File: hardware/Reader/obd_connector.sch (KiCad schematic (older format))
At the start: 2 parts

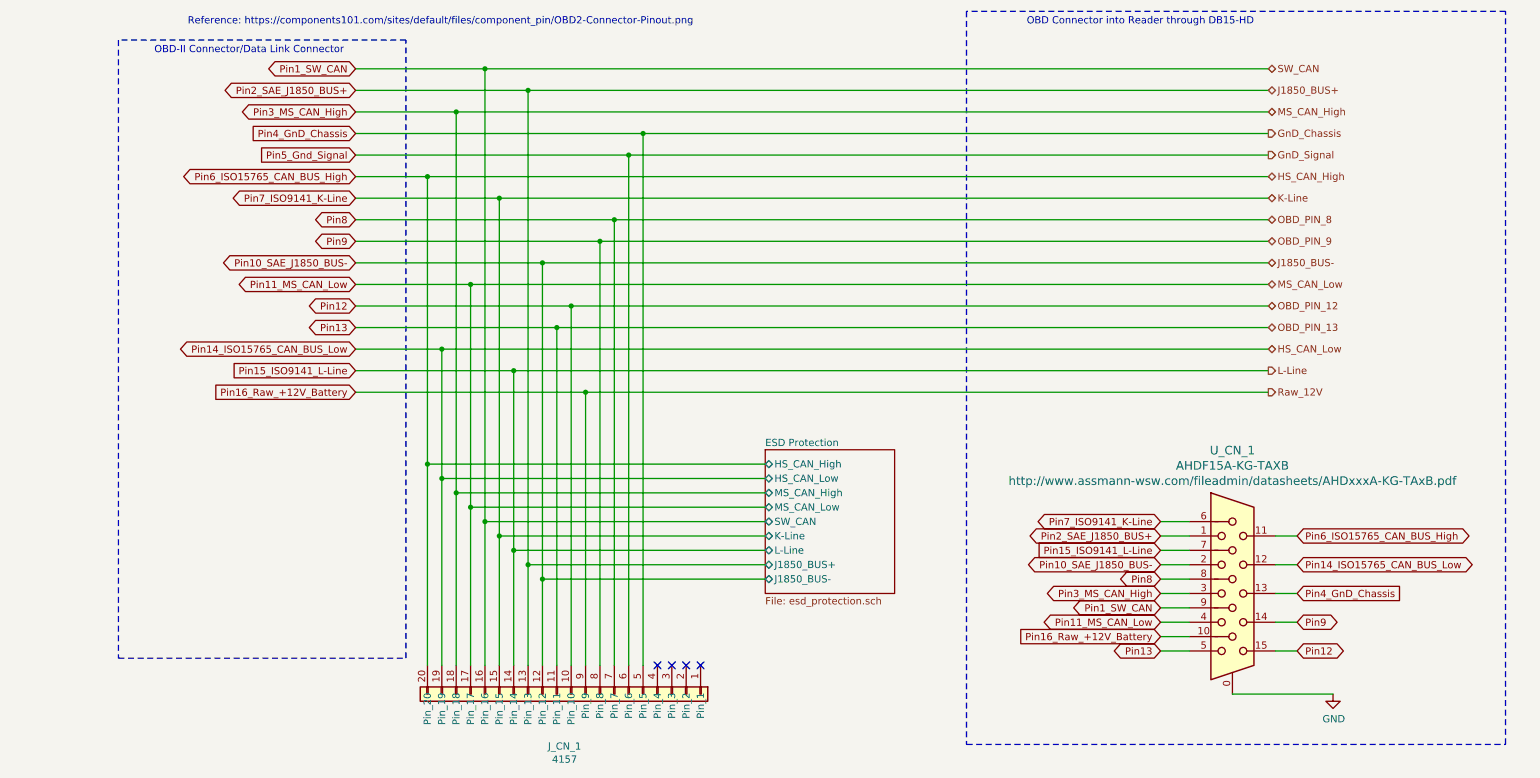
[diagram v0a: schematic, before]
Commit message: Updated reader schematic to v0.0.5 by adding ESP32, removing unused transceivers, fixed design flaws, increased header pins and fixed footprints. Working on reader PCB design
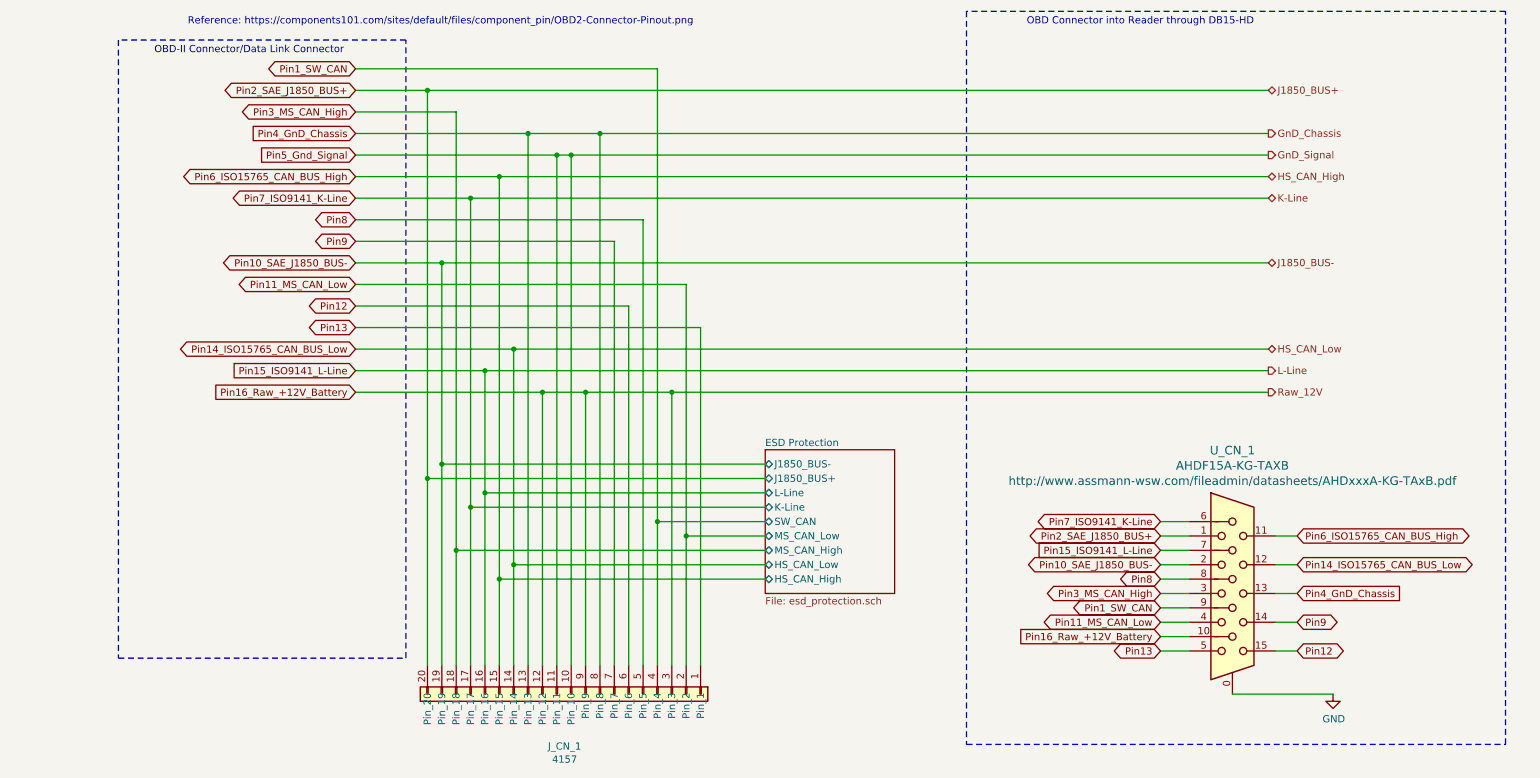
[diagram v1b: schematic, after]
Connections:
- net Pin10_SAE_J1850_BUS-: now also J_CN_1.19 (Pin_19); no longer J_CN_1.12 (Pin_12)
- net Pin11_MS_CAN_Low: now also J_CN_1.2 (Pin_2); no longer J_CN_1.17 (Pin_17)
- net Pin12: now also J_CN_1.6 (Pin_6); no longer J_CN_1.10 (Pin_10)
- net Pin13: now also J_CN_1.1 (Pin_1); no longer J_CN_1.11 (Pin_11)
- net Pin14_ISO15765_CAN_BUS_Low: now also J_CN_1.14 (Pin_14); no longer J_CN_1.19 (Pin_19)
- net Pin15_ISO9141_L-Line: now also J_CN_1.16 (Pin_16); no longer J_CN_1.14 (Pin_14)
- net Pin16_Raw_+12V_Battery: now also J_CN_1.12 (Pin_12), J_CN_1.3 (Pin_3)
- net Pin1_SW_CAN: now also J_CN_1.4 (Pin_4); no longer J_CN_1.16 (Pin_16)
- net Pin2_SAE_J1850_BUS+: now also J_CN_1.20 (Pin_20); no longer J_CN_1.13 (Pin_13)
- net Pin4_GnD_Chassis: now also J_CN_1.13 (Pin_13), J_CN_1.8 (Pin_8); no longer J_CN_1.5 (Pin_5)
- net Pin5_Gnd_Signal: now also J_CN_1.10 (Pin_10), J_CN_1.11 (Pin_11); no longer J_CN_1.6 (Pin_6)
- net Pin6_ISO15765_CAN_BUS_High: now also J_CN_1.15 (Pin_15); no longer J_CN_1.20 (Pin_20)
- net Pin7_ISO9141_K-Line: now also J_CN_1.17 (Pin_17); no longer J_CN_1.15 (Pin_15)
- net Pin8: now also J_CN_1.5 (Pin_5); no longer J_CN_1.7 (Pin_7)
- net Pin9: now also J_CN_1.7 (Pin_7); no longer J_CN_1.8 (Pin_8)
- no-connect marks 4 -> 0
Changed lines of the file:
@@
 $Descr USLetter 11000 8500
 encoding utf-8
-Sheet 11 19
+Sheet 10 17
 Title "CANnect Reader | OBD Connector"
-Date "2020-11-19"
+Date "2020-11-27"
 Rev "0.0.05"
 Comp "CANtech"
@@
 Comment4 "Component Identifier: CN"
 $EndDescr
-Text HLabel 8600 1550 2    50   BiDi ~ 0
-SW_CAN
 Text HLabel 8600 3800 2    50   Output ~ 0
 Raw_12V
 Text HLabel 8600 1700 2    50   BiDi ~ 0
 J1850_BUS+
-Text HLabel 8600 1850 2    50   BiDi ~ 0
-MS_CAN_High
 Text HLabel 8600 2000 2    50   Output ~ 0
 GnD_Chassis
@@
 Text HLabel 8600 2450 2    50   BiDi ~ 0
 K-Line
-Text HLabel 8600 2600 2    50   BiDi ~ 0
-OBD_PIN_8
-Text HLabel 8600 2750 2    50   BiDi ~ 0
-OBD_PIN_9
 Text HLabel 8600 2900 2    50   BiDi ~ 0
 J1850_BUS-
-Text HLabel 8600 3050 2    50   BiDi ~ 0
-MS_CAN_Low
-Text HLabel 8600 3200 2    50   BiDi ~ 0
-OBD_PIN_12
-Text HLabel 8600 3350 2    50   BiDi ~ 0
-OBD_PIN_13
 Text HLabel 8600 3500 2    50   BiDi ~ 0
 HS_CAN_Low
@@
 Wire Notes Line
 	10250 1150 6500 1150
-Wire Wire Line
-	2750 2300 2750 4300
-Wire Wire Line
-	2850 3500 2850 4400
-Wire Wire Line
-	2950 1850 2950 4500
-Wire Wire Line
-	2950 1850 8600 1850
-Wire Wire Line
-	3250 4800 3250 2450
 Wire Notes Line
 	10250 6250 10250 1150
-Connection ~ 2850 3500
-Connection ~ 2750 2300
-Connection ~ 2950 1850
-Wire Wire Line
-	2250 2900 3550 2900
-Wire Wire Line
-	2250 2000 4250 2000
-Wire Wire Line
-	2250 1850 2950 1850
 Text GLabel 2250 2600 0    50   BiDi ~ 0
 Pin8
@@
 Text GLabel 8800 5400 2    50   BiDi ~ 0
 Pin9
-Wire Wire Line
-	2250 2150 4150 2150
-Wire Wire Line
-	2250 2300 2750 2300
-Wire Wire Line
-	2250 2600 4050 2600
-Wire Wire Line
-	2250 2450 3250 2450
-Wire Wire Line
-	2250 3350 3650 3350
-Wire Wire Line
-	2250 3500 2850 3500
 Text GLabel 2250 3650 0    50   Input ~ 0
 Pin15_ISO9141_L-Line
@@
 Text GLabel 7850 4700 0    50   BiDi ~ 0
 Pin7_ISO9141_K-Line
-Wire Wire Line
-	2750 4300 5100 4300
-Wire Wire Line
-	2850 4400 5100 4400
-Wire Wire Line
-	2950 4500 5100 4500
 $Sheet
 S 5100 4200 900  1000
@@
 F0 "ESD Protection" 50
 F1 "esd_protection.sch" 50
-F2 "HS_CAN_High" B L 5100 4300 50
-F3 "HS_CAN_Low" B L 5100 4400 50
-F4 "MS_CAN_High" B L 5100 4500 50
-F5 "MS_CAN_Low" B L 5100 4600 50
+F2 "HS_CAN_High" B L 5100 5100 50
+F3 "HS_CAN_Low" B L 5100 5000 50
+F4 "MS_CAN_High" B L 5100 4900 50
+F5 "MS_CAN_Low" B L 5100 4800 50
 F6 "SW_CAN" B L 5100 4700 50
-F7 "K-Line" B L 5100 4800 50
-F8 "L-Line" B L 5100 4900 50
-F9 "J1850_BUS+" B L 5100 5000 50
-F10 "J1850_BUS-" B L 5100 5100 50
+F7 "K-Line" B L 5100 4600 50
+F8 "L-Line" B L 5100 4500 50
+F9 "J1850_BUS+" B L 5100 4400 50
+F10 "J1850_BUS-" B L 5100 4300 50
 $EndSheet
+Wire Wire Line
+	2250 2000 3450 2000
+Wire Wire Line
+	2250 2150 3650 2150
+Wire Wire Line
+	2250 1550 4350 1550
+Wire Wire Line
+	2250 3800 3550 3800
+Wire Wire Line
+	2250 1700 2750 1700
+Wire Wire Line
+	2250 3350 4650 3350
+Wire Wire Line
+	2250 2900 2850 2900
+Wire Wire Line
+	2250 2750 4050 2750
+Wire Wire Line
+	2250 3650 3150 3650
+Wire Wire Line
+	2250 3500 3350 3500
+Wire Wire Line
+	2250 1850 2950 1850
+Wire Wire Line
+	2250 2300 3250 2300
+Wire Wire Line
+	2250 2450 3050 2450
+Wire Wire Line
+	2250 3050 4550 3050
 $Comp
 L CANtech:4157 J_CN_1
@@
 $EndComp
 Wire Wire Line
-	2750 2300 8600 2300
-Wire Wire Line
-	2850 3500 8600 3500
-Wire Wire Line
-	2750 4300 2750 5700
-Connection ~ 2750 4300
-Wire Wire Line
-	2850 5700 2850 4400
-Connection ~ 2850 4400
-Wire Wire Line
-	2950 4500 2950 5700
-Connection ~ 2950 4500
-Wire Wire Line
-	2250 3050 3050 3050
-Wire Wire Line
-	3050 3050 3050 4600
-Connection ~ 3050 3050
-Wire Wire Line
-	3050 3050 8600 3050
-Wire Wire Line
-	3050 4600 5100 4600
-Connection ~ 3050 4600
-Wire Wire Line
-	3050 4600 3050 5700
-Wire Wire Line
-	2250 1550 3150 1550
-Connection ~ 3150 1550
-Wire Wire Line
-	3150 1550 8600 1550
-Wire Wire Line
-	3150 1550 3150 4700
-Wire Wire Line
-	3150 4700 5100 4700
-Connection ~ 3150 4700
-Wire Wire Line
-	3150 4700 3150 5700
-Connection ~ 3250 2450
-Wire Wire Line
-	3250 2450 8600 2450
-Wire Wire Line
-	3250 4800 5100 4800
-Wire Wire Line
-	3250 4800 3250 5700
-Connection ~ 3250 4800
-Wire Wire Line
-	2250 3650 3350 3650
-Wire Wire Line
-	3350 5700 3350 4900
-Connection ~ 3350 3650
-Wire Wire Line
-	3350 3650 8600 3650
-Wire Wire Line
-	3350 4900 5100 4900
-Connection ~ 3350 4900
-Wire Wire Line
-	3350 4900 3350 3650
-Wire Wire Line
-	2250 1700 3450 1700
-Wire Wire Line
-	3450 1700 3450 5000
-Connection ~ 3450 1700
-Wire Wire Line
-	3450 1700 8600 1700
-Wire Wire Line
-	3450 5000 5100 5000
-Connection ~ 3450 5000
-Wire Wire Line
-	3450 5000 3450 5700
-Connection ~ 3550 2900
-Wire Wire Line
-	3550 2900 8600 2900
-Wire Wire Line
-	3550 2900 3550 5100
-Wire Wire Line
-	3550 5100 5100 5100
-Connection ~ 3550 5100
-Wire Wire Line
-	3550 5100 3550 5700
-Wire Wire Line
-	3650 5700 3650 3350
-Connection ~ 3650 3350
-Wire Wire Line
-	3650 3350 8600 3350
-Wire Wire Line
-	2250 2750 3950 2750
-Wire Wire Line
-	2250 3200 3750 3200
-Wire Wire Line
-	2250 3800 3850 3800
-Wire Wire Line
-	3750 5700 3750 3200
-Connection ~ 3750 3200
-Wire Wire Line
-	3750 3200 8600 3200
+	2750 5700 2750 4400
+Connection ~ 2750 1700
+Wire Wire Line
+	2750 1700 8600 1700
+Wire Wire Line
+	2850 5700 2850 4300
+Connection ~ 2850 2900
+Wire Wire Line
+	2850 2900 8600 2900
+Wire Wire Line
+	2950 5700 2950 4900
+Wire Wire Line
+	3050 5700 3050 4600
+Connection ~ 3050 2450
+Wire Wire Line
+	3050 2450 8600 2450
+Wire Wire Line
+	3150 5700 3150 4500
+Connection ~ 3150 3650
+Wire Wire Line
+	3150 3650 8600 3650
+Wire Wire Line
+	4650 5700 4650 3350
+Wire Wire Line
+	4550 3050 4550 4800
+Wire Wire Line
+	4450 5700 4450 3800
+Connection ~ 4450 3800
+Wire Wire Line
+	4450 3800 8600 3800
+Wire Wire Line
+	4350 5700 4350 4700
+Wire Wire Line
+	4250 5700 4250 2600
+Wire Wire Line
+	2250 2600 4250 2600
+Wire Wire Line
+	4150 5700 4150 3200
+Wire Wire Line
+	2250 3200 4150 3200
+Wire Wire Line
+	4050 5700 4050 2750
+Wire Wire Line
+	3250 5700 3250 5100
+Connection ~ 3250 2300
+Wire Wire Line
+	3250 2300 8600 2300
+Wire Wire Line
+	3350 5700 3350 5000
+Connection ~ 3350 3500
+Wire Wire Line
+	3350 3500 8600 3500
+Wire Wire Line
+	3450 5700 3450 2000
+Connection ~ 3450 2000
+Wire Wire Line
+	3450 2000 3950 2000
+Wire Wire Line
+	3950 5700 3950 2000
+Connection ~ 3950 2000
+Wire Wire Line
+	3950 2000 8600 2000
+Wire Wire Line
+	3550 5700 3550 3800
+Connection ~ 3550 3800
+Wire Wire Line
+	3550 3800 3850 3800
 Wire Wire Line
 	3850 5700 3850 3800
 Connection ~ 3850 3800
 Wire Wire Line
-	3850 3800 8600 3800
-Wire Wire Line
-	3950 5700 3950 2750
-Connection ~ 3950 2750
-Wire Wire Line
-	3950 2750 8600 2750
-Wire Wire Line
-	4050 5700 4050 2600
-Connection ~ 4050 2600
-Wire Wire Line
-	4050 2600 8600 2600
-Wire Wire Line
-	4150 5700 4150 2150
-Connection ~ 4150 2150
-Wire Wire Line
-	4150 2150 8600 2150
-Wire Wire Line
-	4250 2000 4250 5700
-Connection ~ 4250 2000
-Wire Wire Line
-	4250 2000 8600 2000
-NoConn ~ 4350 5700
-NoConn ~ 4450 5700
-NoConn ~ 4550 5700
-NoConn ~ 4650 5700
+	3850 3800 4450 3800
+Wire Wire Line
+	3650 5700 3650 2150
+Connection ~ 3650 2150
+Wire Wire Line
+	3650 2150 3750 2150
+Wire Wire Line
+	3750 2150 3750 5700
+Connection ~ 3750 2150
+Wire Wire Line
+	3750 2150 8600 2150
+Wire Wire Line
+	5100 4300 2850 4300
+Connection ~ 2850 4300
+Wire Wire Line
+	2850 4300 2850 2900
+Wire Wire Line
+	5100 4400 2750 4400
+Connection ~ 2750 4400
+Wire Wire Line
+	2750 4400 2750 1700
+Wire Wire Line
+	5100 4500 3150 4500
+Connection ~ 3150 4500
+Wire Wire Line
+	3150 4500 3150 3650
+Wire Wire Line
+	5100 4600 3050 4600
+Connection ~ 3050 4600
+Wire Wire Line
+	3050 4600 3050 2450
+Wire Wire Line
+	5100 4700 4350 4700
+Connection ~ 4350 4700
+Wire Wire Line
+	4350 4700 4350 1550
+Wire Wire Line
+	5100 4800 4550 4800
+Connection ~ 4550 4800
+Wire Wire Line
+	4550 4800 4550 5700
+Wire Wire Line
+	5100 4900 2950 4900
+Connection ~ 2950 4900
+Wire Wire Line
+	2950 4900 2950 1850
+Wire Wire Line
+	5100 5000 3350 5000
+Connection ~ 3350 5000
+Wire Wire Line
+	3350 5000 3350 3500
+Wire Wire Line
+	5100 5100 3250 5100
+Connection ~ 3250 5100
+Wire Wire Line
+	3250 5100 3250 2300
 $EndSCHEMATC

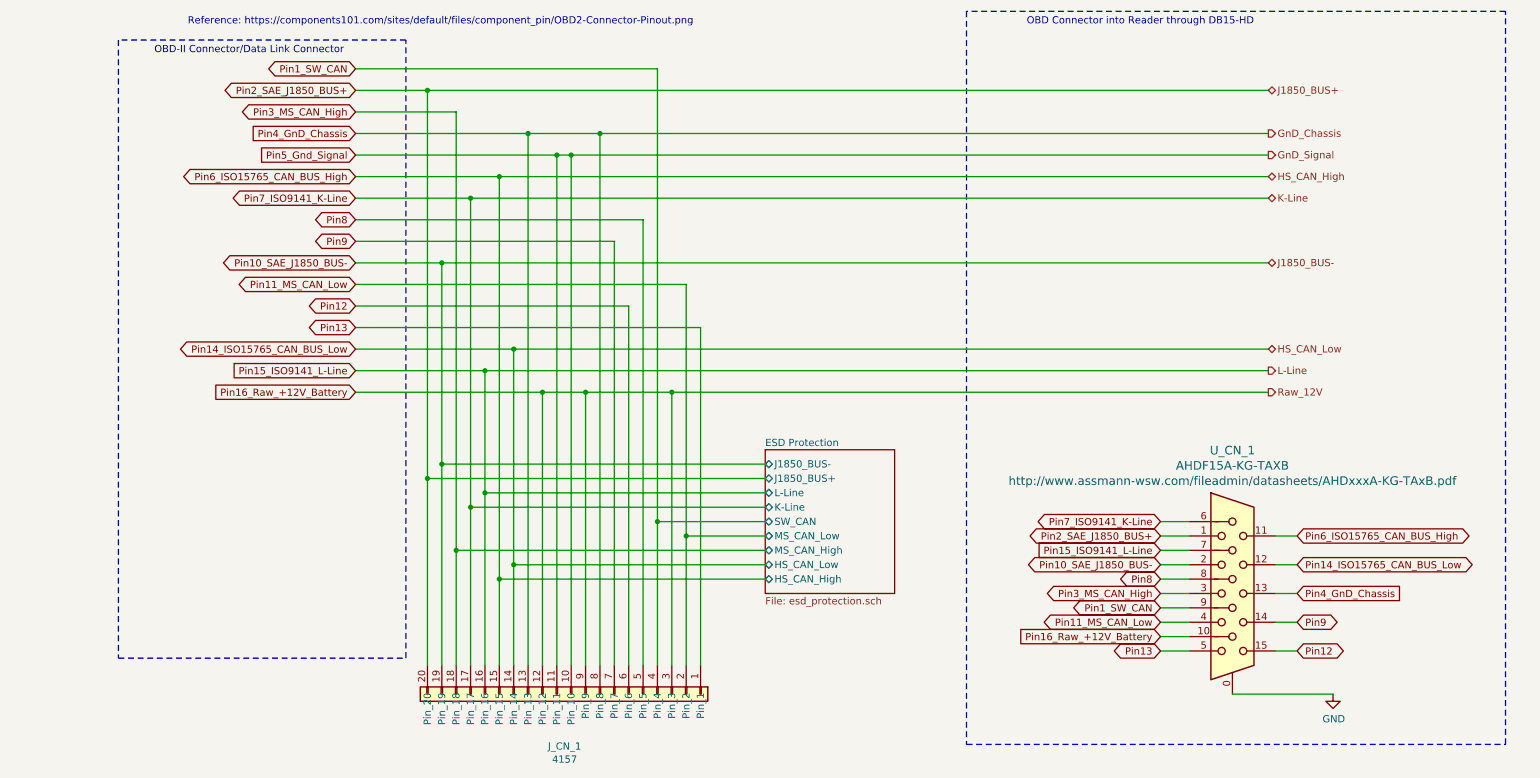
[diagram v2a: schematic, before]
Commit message: Converted PCB design into a 2-layer PCB for v0.0.5b. Adjusted schematic to use header pins for connector
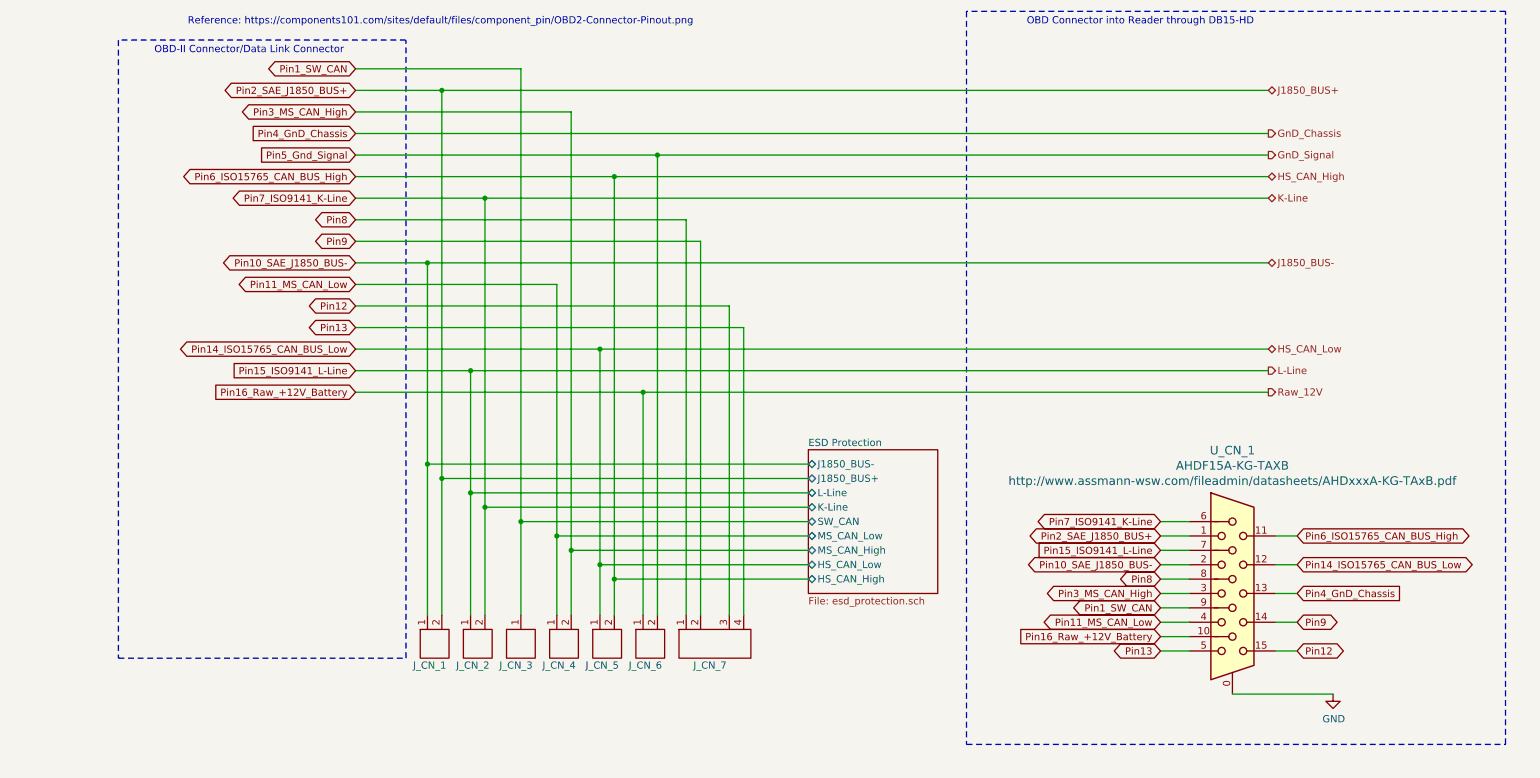
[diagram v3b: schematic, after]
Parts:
- removed J_CN_1: 4157, Connector_PinSocket_2.54mm:PinSocket_1x20_P2.54mm_Vertical, symbol CANtech:4157
- added J_CN_1, J_CN_2, J_CN_4, J_CN_5, J_CN_6: Header_Pin_2, Connector_PinHeader_2.54mm:PinHeader_1x02_P2.54mm_Vertical, symbol CANtech:Header_Pin_2
- added J_CN_3: Header_Pin_1, Connector_PinHeader_2.54mm:PinHeader_1x01_P2.54mm_Vertical, symbol CANtech:Header_Pin_1
- added J_CN_7: Header_Pin_4, Connector_PinHeader_2.54mm:PinHeader_1x04_P2.54mm_Vertical, symbol CANtech:Header_Pin_4
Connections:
- net Pin10_SAE_J1850_BUS-: now also J_CN_1.1
- net Pin11_MS_CAN_Low: now also J_CN_4.1
- net Pin12: now also J_CN_7.3
- net Pin13: now also J_CN_7.4
- net Pin14_ISO15765_CAN_BUS_Low: now also J_CN_5.1
- net Pin15_ISO9141_L-Line: now also J_CN_2.1
- net Pin16_Raw_+12V_Battery: now also J_CN_6.1
- net Pin1_SW_CAN: now also J_CN_3.1
- net Pin2_SAE_J1850_BUS+: now also J_CN_1.2
- net Pin3_MS_CAN_High: now also J_CN_4.2
- net Pin5_Gnd_Signal: now also J_CN_6.2
- net Pin6_ISO15765_CAN_BUS_High: now also J_CN_5.2
- net Pin7_ISO9141_K-Line: now also J_CN_2.2
- net Pin8: now also J_CN_7.1
- net Pin9: now also J_CN_7.2
